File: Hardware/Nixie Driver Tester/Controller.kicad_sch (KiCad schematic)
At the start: 6 parts, among them J1 ICSP, J3 OLED

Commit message: Added Nixie headers
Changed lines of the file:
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@@
 	)
 	(hierarchical_label "5V"
-		(shape bidirectional)
+		(shape input)
 		(at 129.54 78.74 90)
 		(fields_autoplaced yes)
@@
 	)
 	(hierarchical_label "Button"
-		(shape bidirectional)
+		(shape input)
 		(at 162.56 96.52 0)
 		(fields_autoplaced yes)
@@
 	)
 	(hierarchical_label "HVMON"
-		(shape bidirectional)
+		(shape input)
 		(at 162.56 93.98 0)
 		(fields_autoplaced yes)

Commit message: Initial component layout.
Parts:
- R1, R2: footprint Resistor_SMD:R_0201_0603Metric -> Resistor_SMD:R_0603_1608Metric
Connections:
- net GND: now also U1.8 (VSS); no longer U1.20 (VSS)
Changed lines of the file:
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@@
 			)
 		)
-		(property "Footprint" "Resistor_SMD:R_0201_0603Metric"
+		(property "Footprint" "Resistor_SMD:R_0603_1608Metric"
 			(at 109.474 87.884 90)
 			(effects
@@
 		(pin "5"
 		)
-		(pin "20"
+		(pin "8"
 		)
 		(pin "1"
@@
 			)
 		)
-		(property "Footprint" "Resistor_SMD:R_0201_0603Metric"
+		(property "Footprint" "Resistor_SMD:R_0603_1608Metric"
 			(at 118.364 87.884 90)
 			(effects

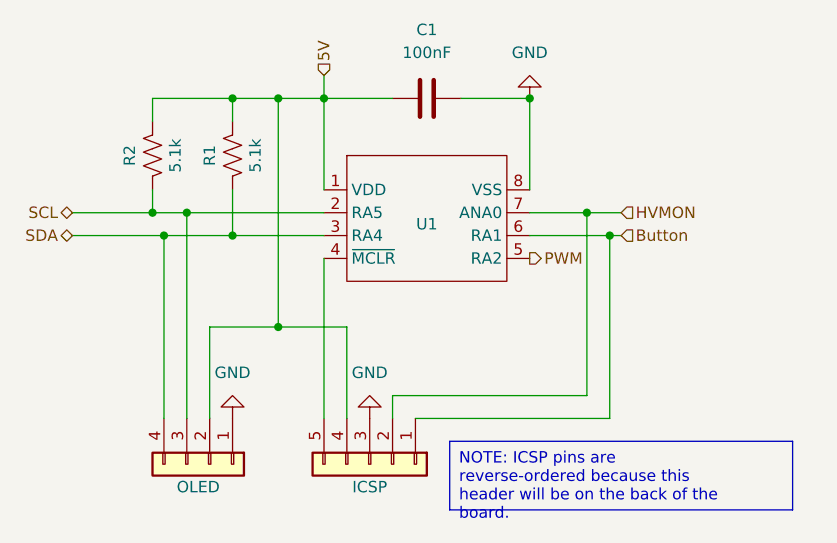
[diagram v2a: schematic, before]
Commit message: Switched to custom OLED symbol/footprint
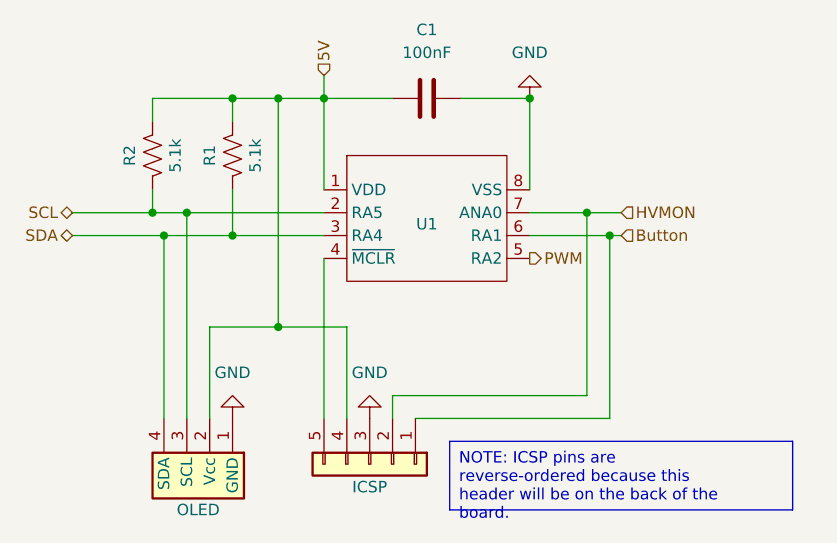
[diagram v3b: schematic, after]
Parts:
- J3: footprint Connector_PinHeader_2.54mm:PinHeader_1x04_P2.54mm_Vertical -> Display_:SSD1306 0.91 128x32 OLED; symbol Connector_Generic:Conn_01x04 -> Display_:SSD1306
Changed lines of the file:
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@@
 		(shape input)
 		(at 129.54 78.74 90)
-		(fields_autoplaced yes)
 		(effects
 			(font
@@
 		(shape input)
 		(at 162.56 96.52 0)
-		(fields_autoplaced yes)
 		(effects
 			(font
@@
 		(shape output)
 		(at 152.4 99.06 0)
-		(fields_autoplaced yes)
 		(effects
 			(font
@@
 		(shape bidirectional)
 		(at 101.6 93.98 180)
-		(fields_autoplaced yes)
 		(effects
 			(font
@@
 		(shape bidirectional)
 		(at 101.6 96.52 180)
-		(fields_autoplaced yes)
 		(effects
 			(font
@@
 		(shape input)
 		(at 162.56 93.98 0)
-		(fields_autoplaced yes)
 		(effects
 			(font
@@
 	)
 	(symbol
-		(lib_id "Connector_Generic:Conn_01x04")
-		(at 116.84 121.92 270)
+		(lib_id "Display_:SSD1306")
+		(at 115.57 120.65 270)
 		(unit 1)
 		(exclude_from_sim no)
@@
 		(dnp no)
 		(property "Reference" "J3"
-			(at 115.57 125.73 90)
+			(at 114.3 124.46 90)
 			(effects
 				(font
@@
 		)
 		(property "Value" "OLED"
-			(at 115.57 124.46 90)
+			(at 115.57 127 90)
 			(effects
 				(font
@@
 			)
 		)
-		(property "Footprint" "Connector_PinHeader_2.54mm:PinHeader_1x04_P2.54mm_Vertical"
-			(at 116.84 121.92 0)
+		(property "Footprint" "Display_:SSD1306 0.91 128x32 OLED"
+			(at 108.966 120.65 0)
 			(effects
 				(font
@@
 		)
 		(property "Datasheet" "~"
-			(at 116.84 121.92 0)
+			(at 115.57 121.92 0)
 			(effects
 				(font
@@
 		)
 		(property "Description" "Generic connector, single row, 01x04, script generated (kicad-library-utils/schlib/autogen/connector/)"
-			(at 116.84 121.92 0)
+			(at 115.57 121.92 0)
 			(effects
 				(font
